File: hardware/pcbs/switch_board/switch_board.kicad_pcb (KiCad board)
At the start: 4 copper layers, 84 x 83 mm, 108 parts, among them J1 8P8C_LED, J2 8P8C_LED, J3 8P8C_LED, J4 8P8C_LED, J5 8P8C_LED, J6 I/O, J8 UART, U2 TPS562231, U3 TPS562231, U4 W25Q32JVSS, U5 24LC64, Y1 TSX-3225

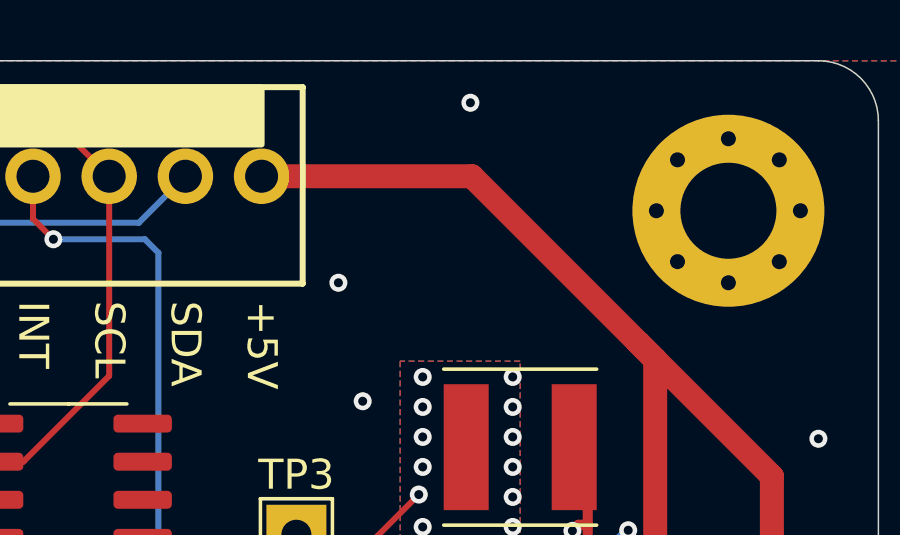
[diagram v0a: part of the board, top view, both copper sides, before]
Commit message: switch_board: add additional power connector
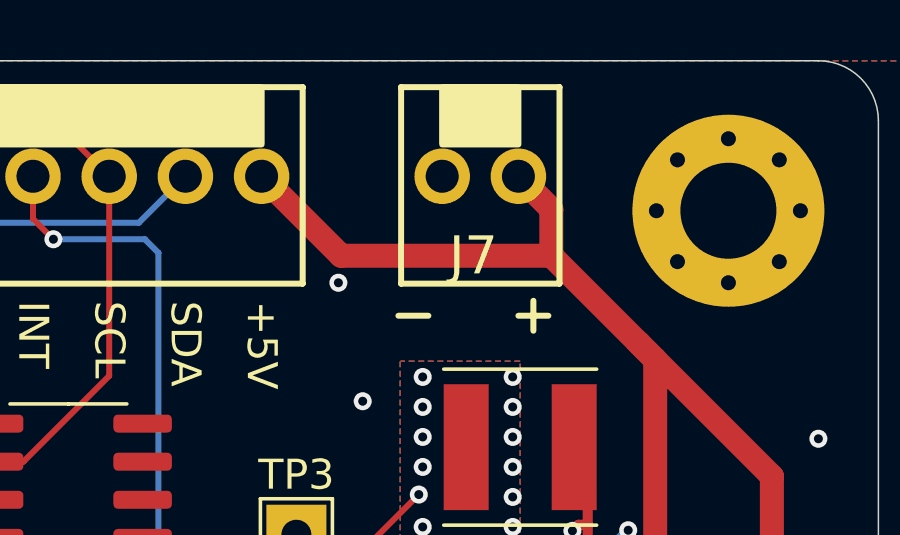
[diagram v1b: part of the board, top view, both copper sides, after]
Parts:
- added J7: Power, Library:mta100_01x2_P2.54_647050-2, F.Cu at (159.0, 62.9)
- U1: value ~ -> RTL8367S
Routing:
- net +5V: track 64.5 -> 67.6 mm

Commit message: boards: update fabrication output settings
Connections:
- net HV_SWR_0 renamed HV_SWR_1

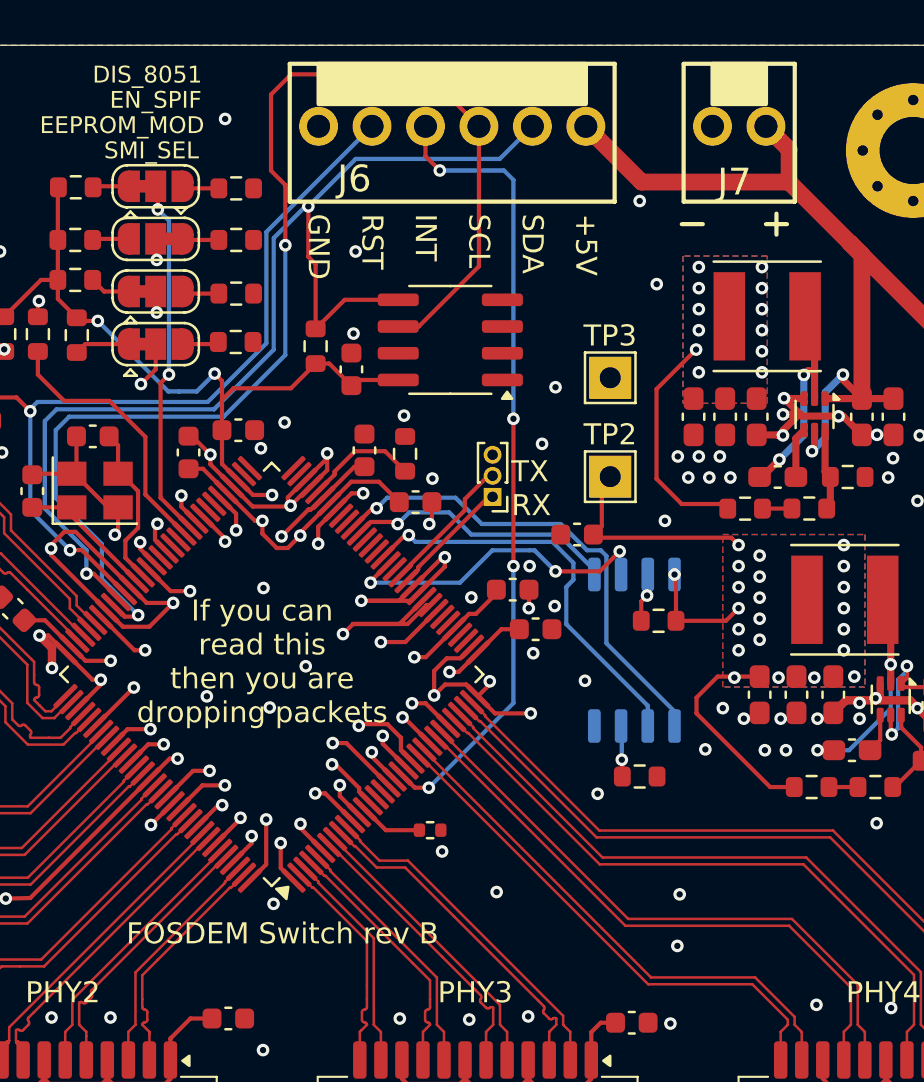
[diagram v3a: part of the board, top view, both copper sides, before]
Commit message: boards: fix many silly bugs discovered during testing
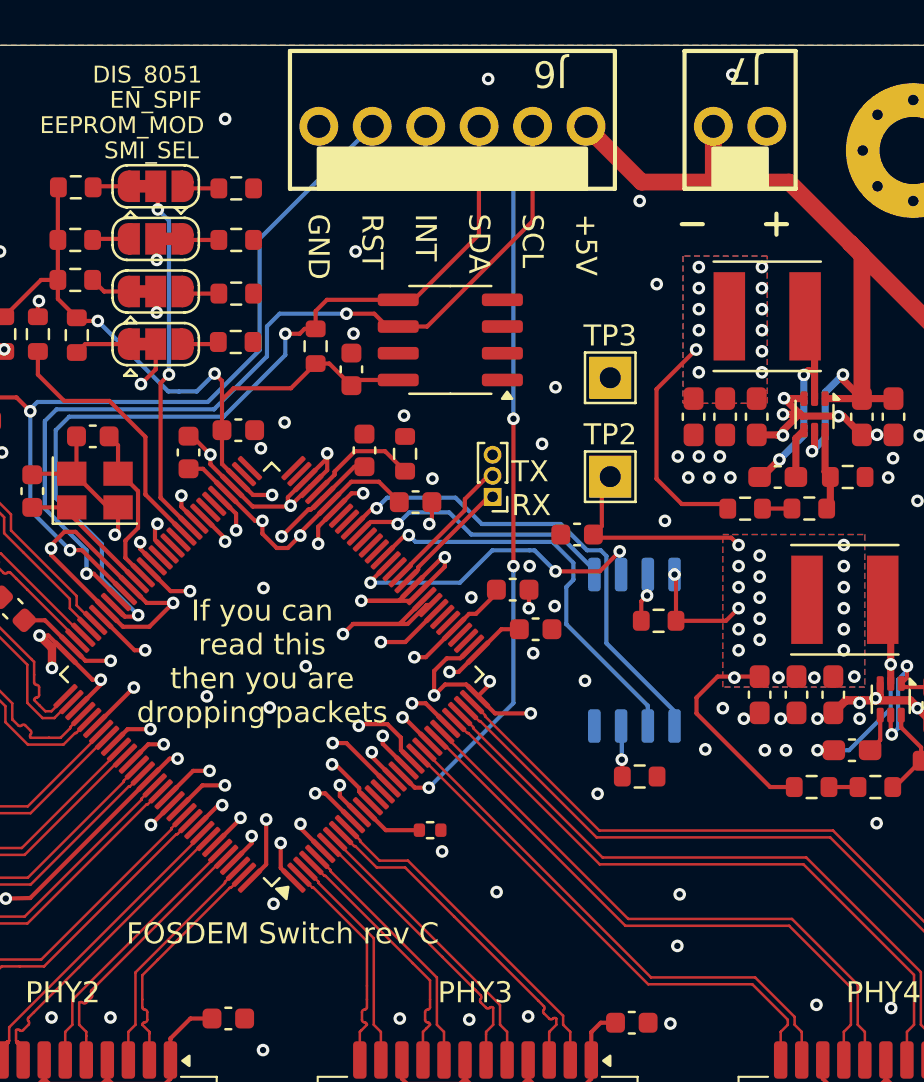
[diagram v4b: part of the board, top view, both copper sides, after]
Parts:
- moved J6 12.7 mm to (137.8, 62.9), turned to 90 degrees
- moved J7 2.50 mm to (156.5, 62.9), turned to 90 degrees
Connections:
- J6 pad 1: +5V -> GND
- J6 pad 2: /SDA -> /RESET
- J6 pad 3: /SCL -> /INT
- J6 pad 4: /INT -> /SDA
- J6 pad 5: /RESET -> /SCL
- J6 pad 6: GND -> +5V
- U1 pad 87: /SDA -> /SCL
- U1 pad 88: /SCL -> /SDA
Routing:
- net /SCL: track 59.9 -> 43.1 mm
- net /SDA: track 52.7 -> 42.1 mm
- net /INT: track 38.2 -> 38.1 mm, vias 4 -> 3
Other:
- board text added: "FOSDEM Switch rev C"
- board text removed: "FOSDEM Switch rev B"
